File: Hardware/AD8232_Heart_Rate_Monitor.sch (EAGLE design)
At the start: 38 parts, among them U1 AD8232

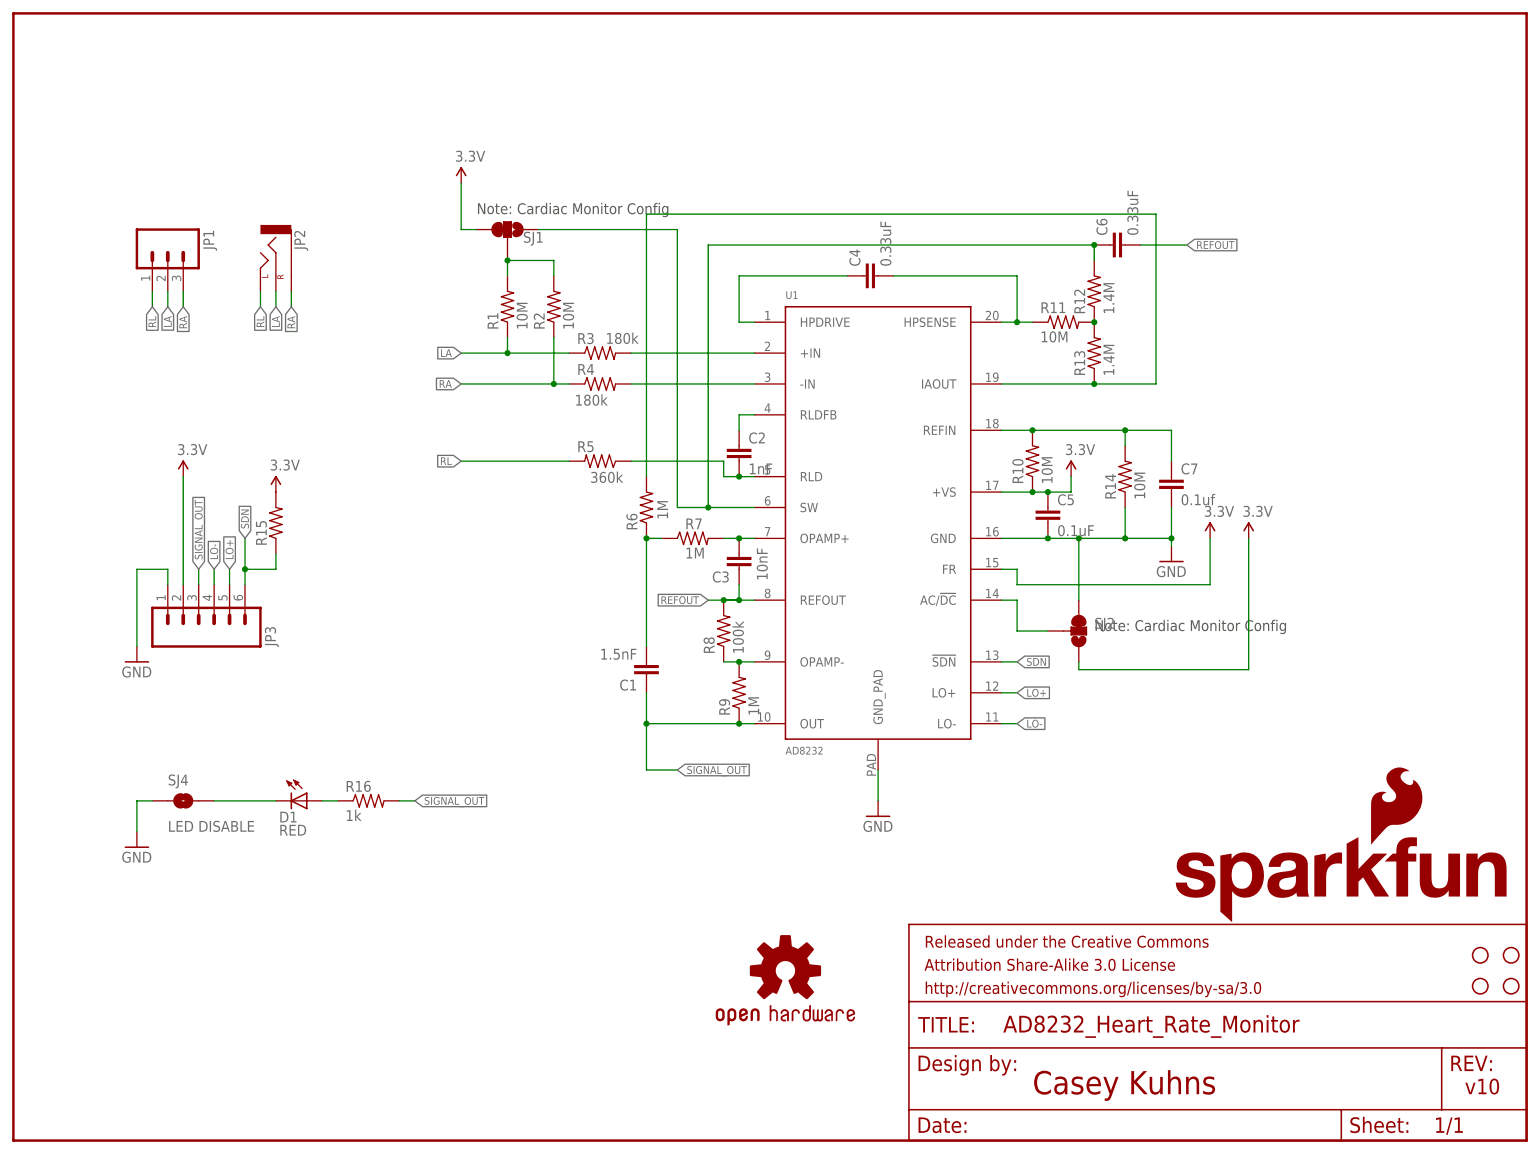
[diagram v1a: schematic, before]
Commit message: changed jumpers to populatable jumpers makes for easy production changes
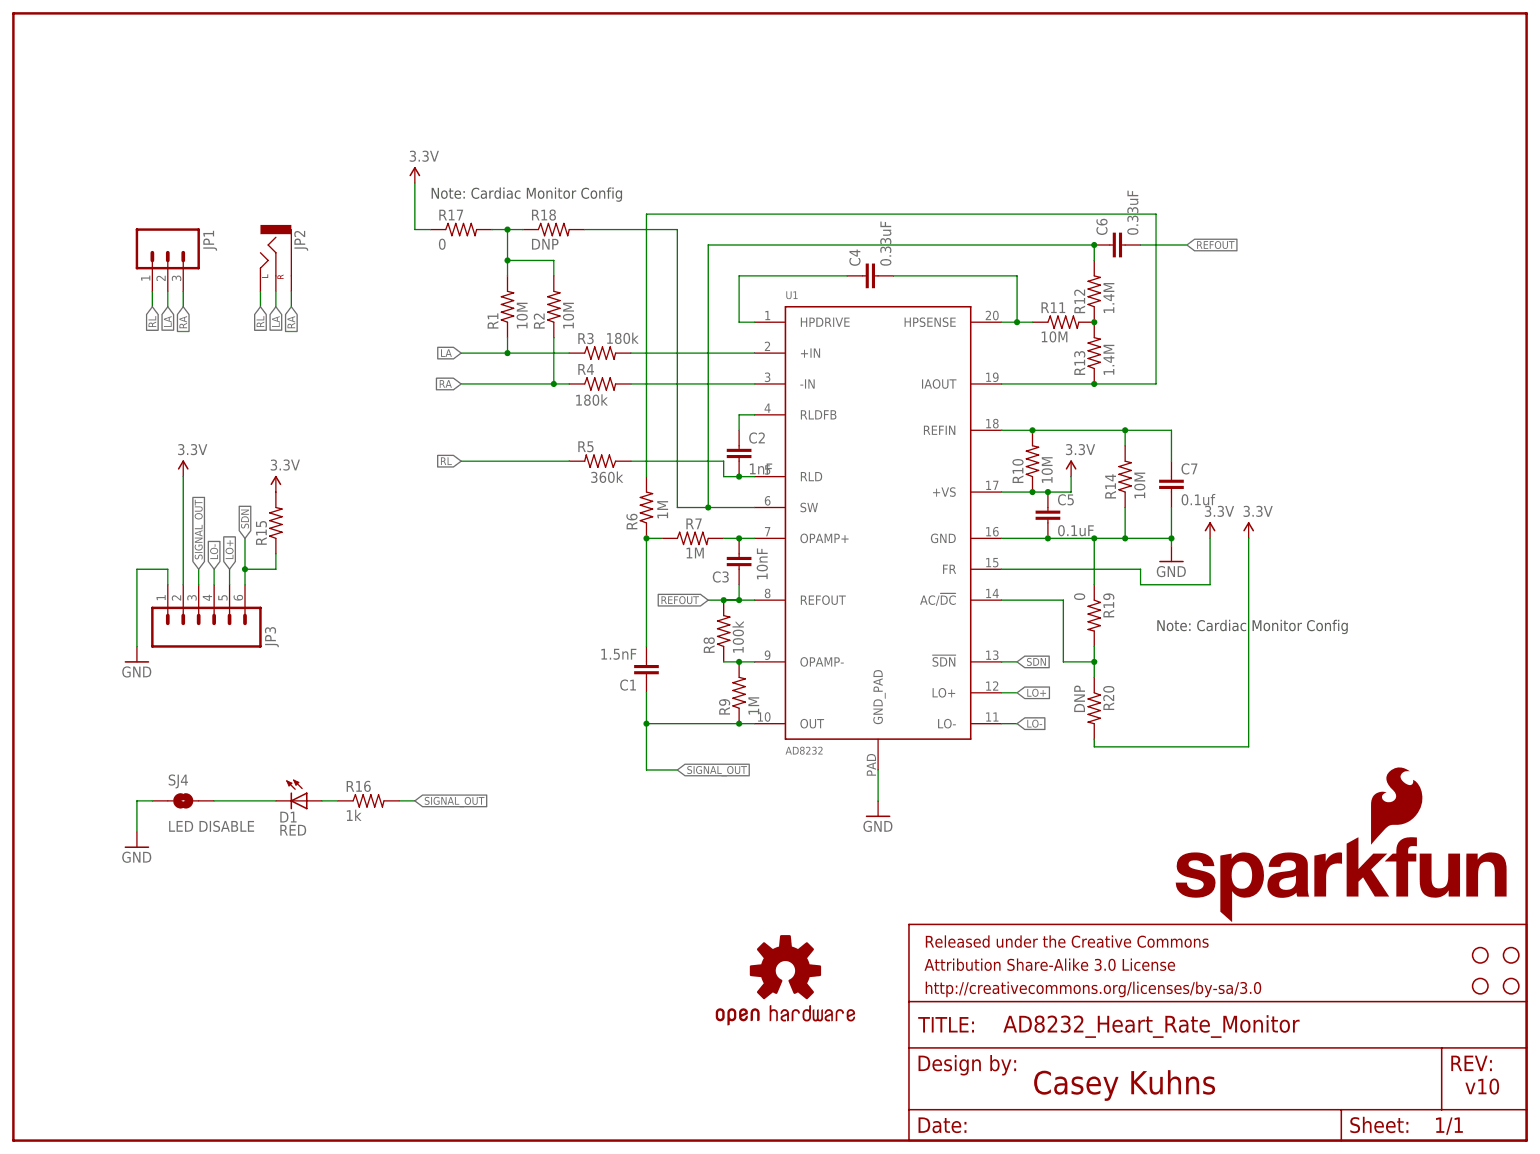
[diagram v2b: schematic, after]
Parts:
- removed SJ1, SJ2: (no value), SparkFun-Passives:SOLDERJUMPER_2WAY-OLDPASTE1&2
- added R17, R19: 0, SparkFun-Resistors:0OHM1/10W5%(0603)
- added R18, R20: DNP, SparkFun-Resistors:0OHM1/10W5%(0603)
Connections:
- removed net N$21: SJ2.2, U1.AC/!DC
- new net N$11: R19.2, R20.1, U1.AC/!DC
- net 3.3V: now also R17.1, R20.2; no longer SJ1.1, SJ2.3
- net GND: now also R19.1; no longer SJ2.1
- net N$16: now also R18.2; no longer SJ1.3
- net N$20: now also R17.2, R18.1; no longer SJ1.2
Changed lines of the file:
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@@
 <part name="GND2" library="SparkFun-Aesthetics" deviceset="GND" device=""/>
 <part name="SUPPLY3" library="SparkFun-Aesthetics" deviceset="3.3V" device=""/>
-<part name="SJ1" library="SparkFun-Passives" deviceset="SOLDERJUMPER_2WAY-OLD" device="PASTE1&amp;2"/>
 <part name="SUPPLY2" library="SparkFun-Aesthetics" deviceset="3.3V" device=""/>
-<part name="SJ2" library="SparkFun-Passives" deviceset="SOLDERJUMPER_2WAY-OLD" device="PASTE1&amp;2"/>
 <part name="SUPPLY4" library="SparkFun-Aesthetics" deviceset="3.3V" device=""/>
 <part name="JP2" library="SparkFun-Connectors" deviceset="AUDIO-JACK" device="SMD2"/>
@@
 <part name="GND4" library="SparkFun-Aesthetics" deviceset="GND" device=""/>
 <part name="SJ4" library="SparkFun-Passives" deviceset="SOLDERJUMPER" device="TRACE" value="LED DISABLE"/>
+<part name="R17" library="SparkFun-Resistors" deviceset="0OHM1/10W5%(0603)" device="" value="0"/>
+<part name="R18" library="SparkFun-Resistors" deviceset="0OHM1/10W5%(0603)" device="" value="DNP"/>
+<part name="R19" library="SparkFun-Resistors" deviceset="0OHM1/10W5%(0603)" device="" value="0"/>
+<part name="R20" library="SparkFun-Resistors" deviceset="0OHM1/10W5%(0603)" device="" value="DNP"/>
 </parts>
 <sheets>
@@
 <text x="167.64" y="7.62" size="3.81" layer="94" font="vector">Casey Kuhns</text>
 <text x="238.76" y="7.62" size="2.54" layer="94" font="vector">v10</text>
-<text x="76.2" y="152.4" size="1.778" layer="97">Note: Cardiac Monitor Config</text>
-<text x="177.8" y="83.82" size="1.778" layer="97">Note: Cardiac Monitor Config</text>
-<wire x1="175.26" y1="85.725" x2="175.26" y2="83.82" width="1.016" layer="94"/>
-<wire x1="81.28" y1="149.86" x2="79.375" y2="149.86" width="1.016" layer="94"/>
+<text x="68.58" y="154.94" size="1.778" layer="97">Note: Cardiac Monitor Config</text>
+<text x="187.96" y="83.82" size="1.778" layer="97">Note: Cardiac Monitor Config</text>
 </plain>
 <instances>
@@
 <instance part="GND2" gate="1" x="190.5" y="95.25"/>
 <instance part="SUPPLY3" gate="G$1" x="196.85" y="99.06"/>
-<instance part="SJ1" gate="G$1" x="81.28" y="149.86" smashed="yes" rot="R90">
-<attribute name="NAME" x="83.82" y="147.701" size="1.778" layer="95"/>
-<attribute name="VALUE" x="83.185" y="152.4" size="1.778" layer="96" rot="R90"/>
-</instance>
-<instance part="SUPPLY2" gate="G$1" x="73.66" y="157.48"/>
-<instance part="SJ2" gate="G$1" x="175.26" y="83.82"/>
+<instance part="SUPPLY2" gate="G$1" x="66.04" y="157.48"/>
 <instance part="SUPPLY4" gate="G$1" x="203.2" y="99.06"/>
 <instance part="JP2" gate="G$1" x="43.18" y="144.78" rot="R270"/>
@@
 <instance part="GND4" gate="1" x="20.32" y="48.26"/>
 <instance part="SJ4" gate="1" x="27.94" y="55.88"/>
+<instance part="R17" gate="G$1" x="73.66" y="149.86"/>
+<instance part="R18" gate="G$1" x="88.9" y="149.86"/>
+<instance part="R19" gate="G$1" x="177.8" y="86.36" rot="R270"/>
+<instance part="R20" gate="G$1" x="177.8" y="71.12" rot="R270"/>
 </instances>
 <busses>
@@
 <pinref part="C5" gate="G$1" pin="2"/>
 <wire x1="162.56" y1="99.06" x2="170.18" y2="99.06" width="0.1524" layer="91"/>
-<wire x1="170.18" y1="99.06" x2="175.26" y2="99.06" width="0.1524" layer="91"/>
-<wire x1="175.26" y1="99.06" x2="182.88" y2="99.06" width="0.1524" layer="91"/>
+<wire x1="170.18" y1="99.06" x2="177.8" y2="99.06" width="0.1524" layer="91"/>
+<wire x1="177.8" y1="99.06" x2="182.88" y2="99.06" width="0.1524" layer="91"/>
 <wire x1="182.88" y1="99.06" x2="190.5" y2="99.06" width="0.1524" layer="91"/>
 <junction x="170.18" y="99.06"/>
@@
 <wire x1="190.5" y1="99.06" x2="190.5" y2="97.79" width="0.1524" layer="91"/>
 <junction x="190.5" y="99.06"/>
-<pinref part="SJ2" gate="G$1" pin="1"/>
-<wire x1="175.26" y1="88.9" x2="175.26" y2="99.06" width="0.1524" layer="91"/>
-<junction x="175.26" y="99.06"/>
+<wire x1="177.8" y1="91.44" x2="177.8" y2="99.06" width="0.1524" layer="91"/>
+<junction x="177.8" y="99.06"/>
+<pinref part="R19" gate="G$1" pin="1"/>
 </segment>
 <segment>
@@
 <wire x1="114.3" y1="147.32" x2="177.8" y2="147.32" width="0.1524" layer="91"/>
 <junction x="177.8" y="147.32"/>
-<pinref part="SJ1" gate="G$1" pin="3"/>
-<wire x1="86.36" y1="149.86" x2="109.22" y2="149.86" width="0.1524" layer="91"/>
+<wire x1="93.98" y1="149.86" x2="109.22" y2="149.86" width="0.1524" layer="91"/>
 <wire x1="109.22" y1="149.86" x2="109.22" y2="104.14" width="0.1524" layer="91"/>
 <wire x1="109.22" y1="104.14" x2="114.3" y2="104.14" width="0.1524" layer="91"/>
 <junction x="114.3" y="104.14"/>
+<pinref part="R18" gate="G$1" pin="2"/>
 </segment>
 </net>
@@
 <segment>
 <pinref part="U1" gate="U$1" pin="FR"/>
-<wire x1="162.56" y1="93.98" x2="165.1" y2="93.98" width="0.1524" layer="91"/>
-<wire x1="165.1" y1="93.98" x2="165.1" y2="91.44" width="0.1524" layer="91"/>
-<wire x1="165.1" y1="91.44" x2="196.85" y2="91.44" width="0.1524" layer="91"/>
+<wire x1="162.56" y1="93.98" x2="185.42" y2="93.98" width="0.1524" layer="91"/>
+<wire x1="185.42" y1="93.98" x2="185.42" y2="91.44" width="0.1524" layer="91"/>
+<wire x1="185.42" y1="91.44" x2="196.85" y2="91.44" width="0.1524" layer="91"/>
 <wire x1="196.85" y1="91.44" x2="196.85" y2="99.06" width="0.1524" layer="91"/>
 <pinref part="SUPPLY3" gate="G$1" pin="3.3V"/>
 </segment>
 <segment>
-<pinref part="SJ1" gate="G$1" pin="1"/>
 <pinref part="SUPPLY2" gate="G$1" pin="3.3V"/>
-<wire x1="73.66" y1="157.48" x2="73.66" y2="149.86" width="0.1524" layer="91"/>
-<wire x1="73.66" y1="149.86" x2="76.2" y2="149.86" width="0.1524" layer="91"/>
-</segment>
-<segment>
-<pinref part="SJ2" gate="G$1" pin="3"/>
-<wire x1="175.26" y1="78.74" x2="175.26" y2="77.47" width="0.1524" layer="91"/>
-<wire x1="175.26" y1="77.47" x2="203.2" y2="77.47" width="0.1524" layer="91"/>
-<wire x1="203.2" y1="77.47" x2="203.2" y2="99.06" width="0.1524" layer="91"/>
+<wire x1="66.04" y1="157.48" x2="66.04" y2="149.86" width="0.1524" layer="91"/>
+<wire x1="66.04" y1="149.86" x2="68.58" y2="149.86" width="0.1524" layer="91"/>
+<pinref part="R17" gate="G$1" pin="1"/>
+</segment>
+<segment>
+<wire x1="177.8" y1="66.04" x2="177.8" y2="64.77" width="0.1524" layer="91"/>
+<wire x1="177.8" y1="64.77" x2="203.2" y2="64.77" width="0.1524" layer="91"/>
+<wire x1="203.2" y1="64.77" x2="203.2" y2="99.06" width="0.1524" layer="91"/>
 <pinref part="SUPPLY4" gate="G$1" pin="3.3V"/>
+<pinref part="R20" gate="G$1" pin="2"/>
 </segment>
 <segment>
@@
 <pinref part="R2" gate="G$1" pin="2"/>
 <wire x1="88.9" y1="144.78" x2="88.9" y2="142.24" width="0.1524" layer="91"/>
-<pinref part="SJ1" gate="G$1" pin="2"/>
+<pinref part="R17" gate="G$1" pin="2"/>
+<pinref part="R18" gate="G$1" pin="1"/>
+<wire x1="83.82" y1="149.86" x2="81.28" y2="149.86" width="0.1524" layer="91"/>
+<wire x1="81.28" y1="149.86" x2="78.74" y2="149.86" width="0.1524" layer="91"/>
+<wire x1="81.28" y1="144.78" x2="81.28" y2="149.86" width="0.1524" layer="91"/>
 <junction x="81.28" y="144.78"/>
-</segment>
-</net>
-<net name="N$21" class="0">
-<segment>
-<pinref part="U1" gate="U$1" pin="AC/!DC"/>
-<wire x1="162.56" y1="88.9" x2="165.1" y2="88.9" width="0.1524" layer="91"/>
-<wire x1="165.1" y1="88.9" x2="165.1" y2="83.82" width="0.1524" layer="91"/>
-<pinref part="SJ2" gate="G$1" pin="2"/>
-<wire x1="165.1" y1="83.82" x2="170.18" y2="83.82" width="0.1524" layer="91"/>
+<junction x="81.28" y="149.86"/>
 </segment>
 </net>
@@
 </segment>
 </net>
+<net name="N$11" class="0">
+<segment>
+<pinref part="U1" gate="U$1" pin="AC/!DC"/>
+<wire x1="162.56" y1="88.9" x2="172.72" y2="88.9" width="0.1524" layer="91"/>
+<wire x1="172.72" y1="88.9" x2="172.72" y2="78.74" width="0.1524" layer="91"/>
+<pinref part="R19" gate="G$1" pin="2"/>
+<pinref part="R20" gate="G$1" pin="1"/>
+<wire x1="177.8" y1="76.2" x2="177.8" y2="78.74" width="0.1524" layer="91"/>
+<wire x1="177.8" y1="78.74" x2="177.8" y2="81.28" width="0.1524" layer="91"/>
+<wire x1="172.72" y1="78.74" x2="177.8" y2="78.74" width="0.1524" layer="91"/>
+<junction x="177.8" y="78.74"/>
+</segment>
+</net>
